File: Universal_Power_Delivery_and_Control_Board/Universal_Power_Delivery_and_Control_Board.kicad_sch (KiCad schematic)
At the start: 1 part

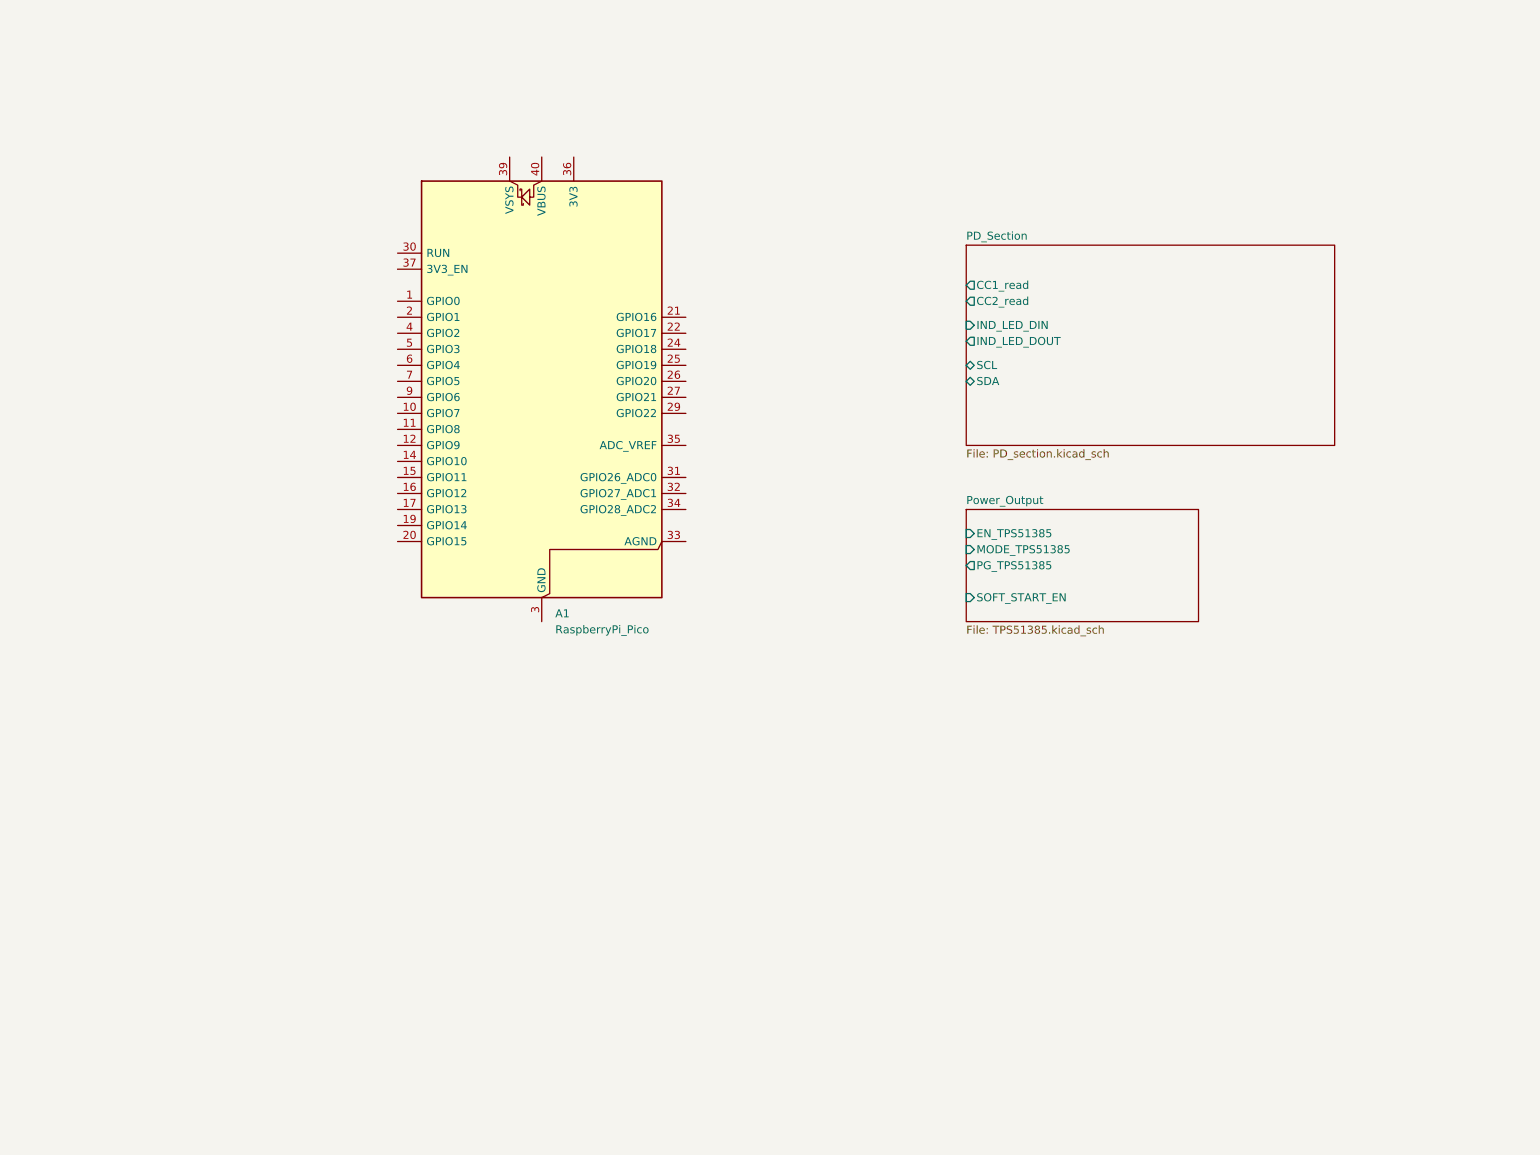
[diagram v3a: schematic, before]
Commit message: Restructured the schematic, added the digital output section and continued with the layout.
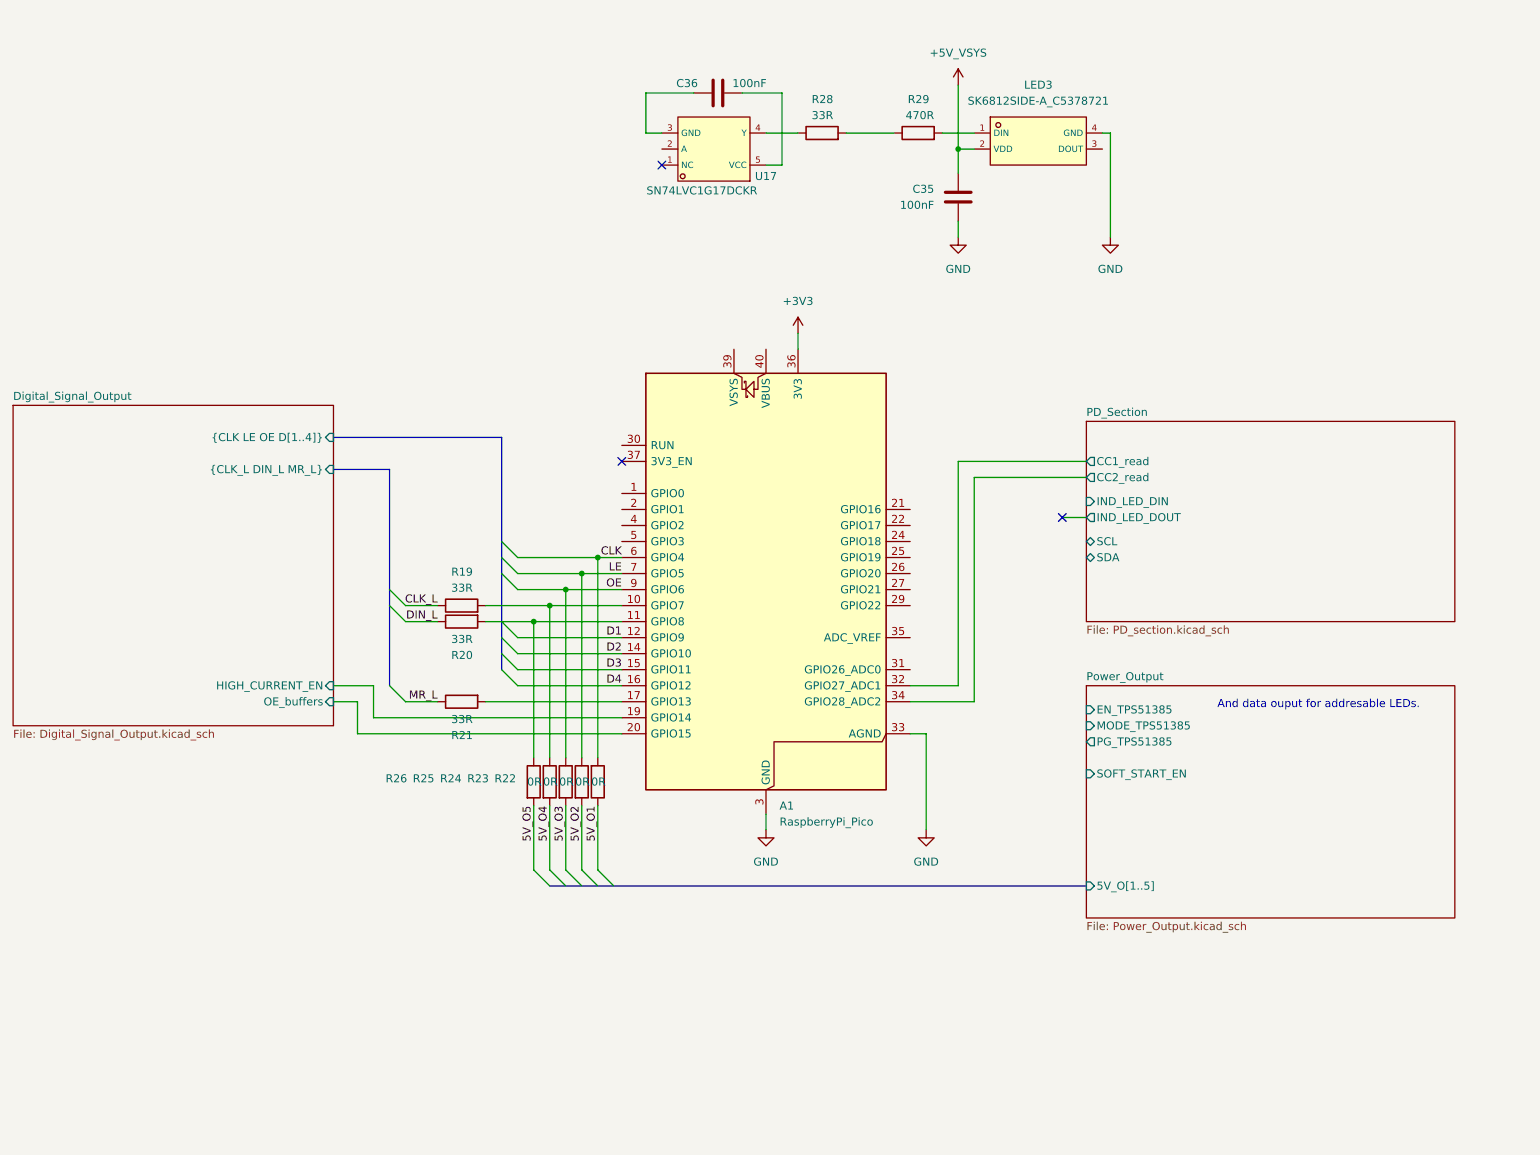
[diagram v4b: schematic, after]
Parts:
- added C35, C36: 100nF, Capacitor_SMD:C_0402_1005Metric_Pad0.74x0.62mm_HandSolder, symbol Device:C
- added LED3: SK6812SIDE-A_C5378721, lcsc_footprints:C5378721_LED-SMD_4P-L4_0-W1_6-L, symbol lcsc_imported:SK6812SIDE-A_C5378721
- added R19, R20, R21, R28: 33R, Resistor_SMD:R_0402_1005Metric_Pad0.72x0.64mm_HandSolder, symbol Device:R
- added R22, R23, R24, R25, R26: 0R, Resistor_SMD:R_0402_1005Metric_Pad0.72x0.64mm_HandSolder, symbol Device:R
- added R29: 470R, Resistor_SMD:R_0402_1005Metric_Pad0.72x0.64mm_HandSolder, symbol Device:R
- added U17: SN74LVC1G17DCKR, lcsc_footprints:C10425_SC-70-5_L2_1-W1_3-P0_65-LS2_1-BR, symbol lcsc_imported:SN74LVC1G17DCKR
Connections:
- net PD_Section/CC1_read: now also A1.32 (GPIO27_ADC1)
- net PD_Section/CC2_read: now also A1.34 (GPIO28_ADC2)
- net at A1.10 (GPIO7): now also R19.2, R25.1
- net at A1.11 (GPIO8): now also R20.2, R26.1
- net D1: now reaches A1.12 (GPIO9)
- net GND: now reaches A1.13 (GND), A1.18 (GND), A1.23 (GND), A1.28 (GND), A1.3 (GND), A1.38 (GND), A1.8 (GND)
- net GND: now also A1.33 (AGND), C35.2, LED3.4 (GND)
- net D2: now reaches A1.14 (GPIO10)
- net D3: now reaches A1.15 (GPIO11)
- net D4: now reaches A1.16 (GPIO12)
- net at A1.17 (GPIO13): now also R21.2
- net Digital_Signal_Output/HIGH_CURRENT_EN: now reaches A1.19 (GPIO14)
- net Digital_Signal_Output/OE_buffers: now reaches A1.20 (GPIO15)
- net +3V3: now reaches A1.36 (3V3)
- net CLK: now reaches A1.6 (GPIO4)
- net CLK: now also R22.2
- net LE: now reaches A1.7 (GPIO5)
- net LE: now also R23.1
- net OE: now reaches A1.9 (GPIO6)
- net OE: now also R24.1
- new net: C36.1, U17.5 (VCC)
- new net: C36.2, U17.3 (GND)
- new net: R28.2, R29.1
- new net: LED3.1 (DIN), R29.2
- new net: R28.1, U17.4 (Y)
- new net +5V_VSYS: C35.1, LED3.2 (VDD)
- new net 5V_O1: R22.1
- new net 5V_O2: R23.2
- new net 5V_O3: R24.2
- new net 5V_O4: R25.2
- new net 5V_O5: R26.2
- new net CLK_L: R19.1
- new net DIN_L: R20.1
- new net MR_L: R21.1
- no-connect marks 0 -> 3
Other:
- added sheet Digital_Signal_Output (Digital_Signal_Output.kicad_sch)
- sheet Power_Output: file TPS51385.kicad_sch -> Power_Output.kicad_sch
- sheet Power_Output ports: added 5V_O[1..5]; removed none
- note added: "And data ouput for addresable LEDs."
- moved on the sheet: A1

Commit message: Switched to a 4 layer stackup and routed the digital output section.
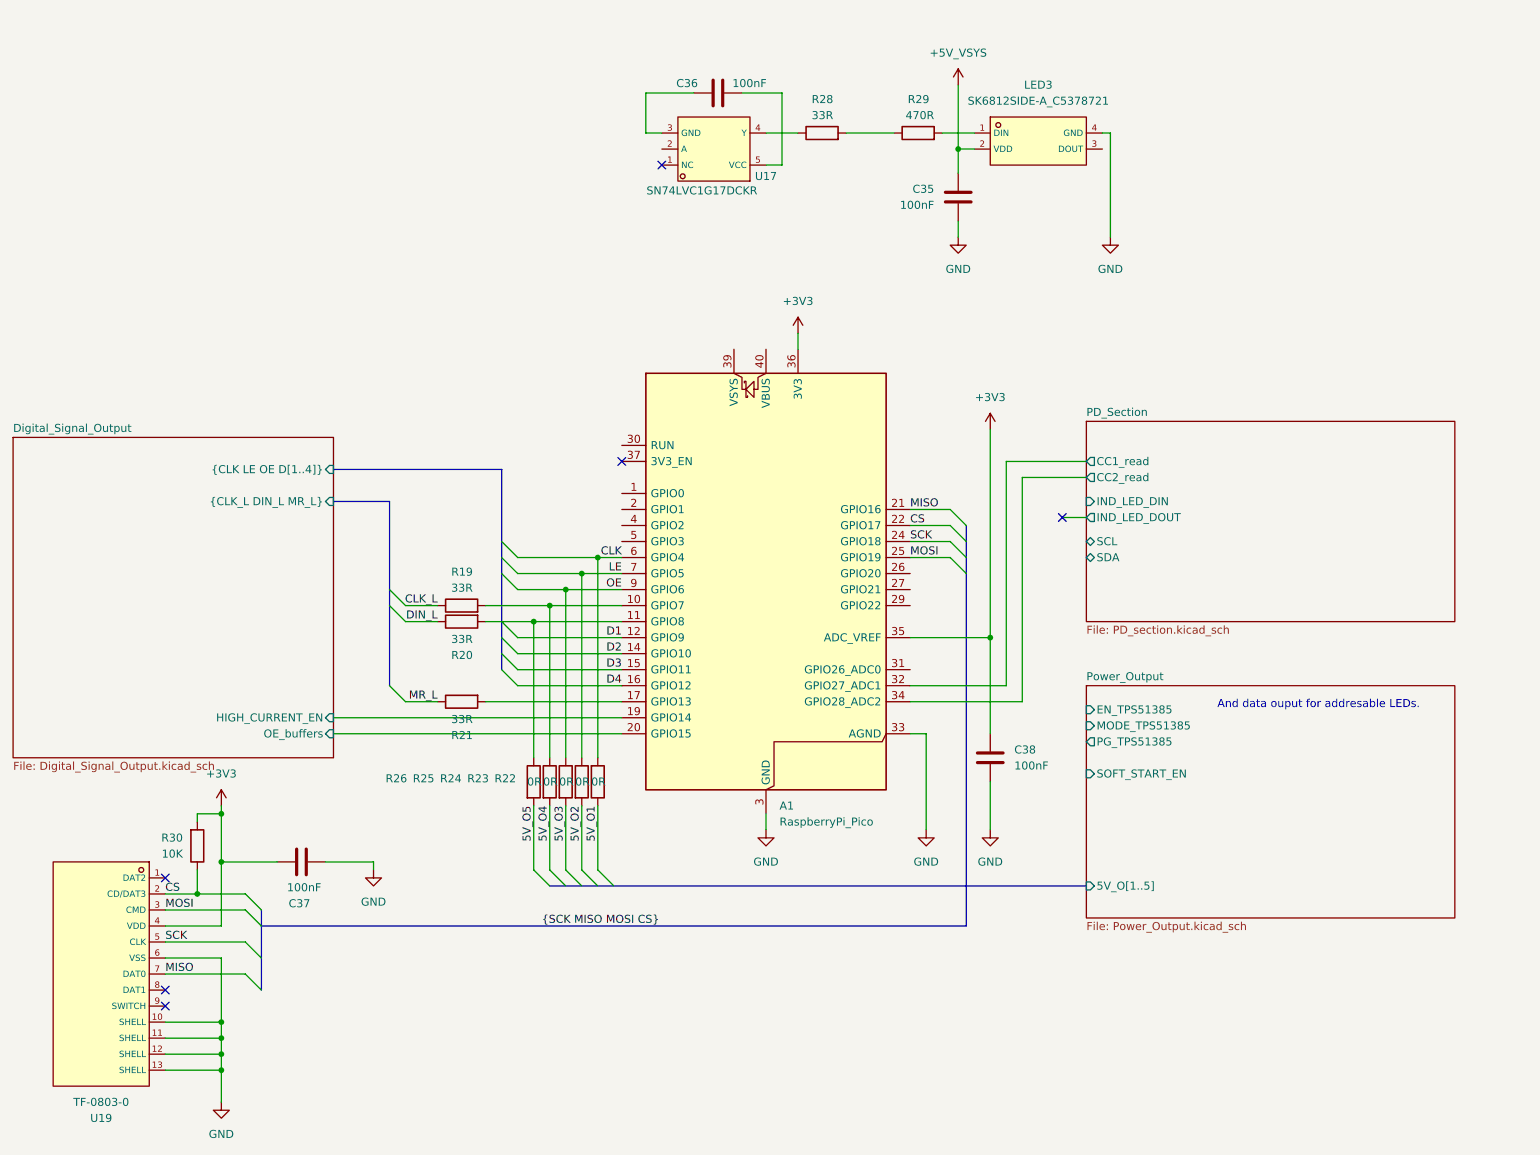
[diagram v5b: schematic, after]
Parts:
- added C37, C38: 100nF, Capacitor_SMD:C_0402_1005Metric_Pad0.74x0.62mm_HandSolder, symbol Device:C
- added R30: 10K, Resistor_SMD:R_0402_1005Metric_Pad0.72x0.64mm_HandSolder, symbol Device:R
- added U19: TF-0803-0, lcsc_footprints:C5362199_TF-SMD_XKTF-0803-0, symbol lcsc_imported:TF-0803-0
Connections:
- net +3V3: now also A1.35 (ADC_VREF), C37.1, C38.1, R30.2, U19.4 (VDD)
- net GND: now also C37.2, C38.2, U19.10 (SHELL), U19.11 (SHELL), U19.12 (SHELL), U19.13 (SHELL), U19.6 (VSS)
- net MISO: now reaches A1.21 (GPIO16)
- net MISO: now also U19.7 (DAT0)
- net CS: now reaches A1.22 (GPIO17)
- net CS: now also R30.1, U19.2 (CD/DAT3)
- net SCK: now reaches A1.24 (GPIO18)
- net SCK: now also U19.5 (CLK)
- net MOSI: now reaches A1.25 (GPIO19)
- net MOSI: now also U19.3 (CMD)
- no-connect marks 3 -> 6

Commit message: Practically finshed the digital output layout, added the i2c io expander as im short on ios.
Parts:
- removed R22, R23, R24, R25, R26: 0R, Resistor_SMD:R_0402_1005Metric_Pad0.72x0.64mm_HandSolder, symbol Device:R
- added C42: 100nF, Capacitor_SMD:C_0402_1005Metric_Pad0.74x0.62mm_HandSolder, symbol Device:C
- added C43: 10uF, Capacitor_SMD:C_0805_2012Metric_Pad1.18x1.45mm_HandSolder, symbol Device:C
- added JP5, JP6: SolderJumper_3_Bridged12, Jumper:SolderJumper-3_P1.3mm_Bridged12_Pad1.0x1.5mm_NumberLabels, symbol Jumper:SolderJumper_3_Bridged12
- added U20: TCA9555PWR, Package_SO:TSSOP-24_4.4x7.8mm_P0.65mm, symbol Interface_Expansion:TCA9555PWR
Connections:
- net CLK is gone; now on net 5V_O1: A1.6 (GPIO4)
- net LE is gone; now on net 5V_O2: A1.7 (GPIO5)
- net OE is gone; now on net 5V_O3: A1.9 (GPIO6)
- net +3V3: now also C42.1, C43.2, JP5.3 (B), JP6.3 (B), U20.24 (VCC)
- net +5V_VSYS: now also A1.39 (VSYS)
- net 5V_O4: now also A1.10 (GPIO7), R19.2
- net 5V_O5: now also A1.11 (GPIO8), R20.2
- net GND: now also C42.2, C43.1, JP5.1 (A), JP6.1 (A), U20.12 (GND), U20.21 (A0)
- net SDA: now reaches A1.1 (GPIO0)
- net SDA: now also U20.22 (SCL)
- net SCL: now reaches A1.2 (GPIO1)
- net SCL: now also U20.23 (SDA)
- net INT: now reaches A1.4 (GPIO2)
- net INT: now also U20.1 (~{INT})
- new net: JP6.2 (C), U20.2 (A1)
- new net: JP5.2 (C), U20.3 (A2)

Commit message: Added some misc stuff layout almost finished.
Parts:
- removed R28: 33R, Resistor_SMD:R_0402_1005Metric_Pad0.72x0.64mm_HandSolder, symbol Device:R
- added R25, R26: 4.7K, Resistor_SMD:R_0402_1005Metric_Pad0.72x0.64mm_HandSolder, symbol Device:R
- added SW2: TS1102-TD35HBM, lcsc_footprints:C36936640_SW-SMD_TS1102-TD35HBM, symbol lcsc_imported:TS1102-TD35HBM
- added U22: HC-PM254-8.5H-2X4PW-02A, lcsc_footprints:C42163146_HDR-TH_8P-P2_54-H-F-R2-C4-S2_54-W8_5, symbol lcsc_imported:HC-PM254-8_5H-2X4PW-02A
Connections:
- net +3V3: now also R25.2, R26.2, U22.2
- net GND: now also U22.1
- net SCL: now also R25.1
- net SDA: now also R26.1
- net at U20.13 (P10): now also U22.4
- net at U20.14 (P11): now also U22.6
- net at U20.15 (P12): now also U22.8
- net at U20.16 (P13): now also U22.7
- net at U20.17 (P14): now also U22.5
- net at U20.18 (P15): now also U22.3
- net P00: now reaches U20.4 (P00)
- net P01: now reaches U20.5 (P01)
- net P02: now reaches U20.6 (P02)
- net P03: now reaches U20.7 (P03)
- net P04: now reaches U20.8 (P04)
- net P05: now reaches U20.9 (P05)
- net SS_EN: now reaches A1.5 (GPIO3)
- net at R29.1: now also U17.4 (Y)
- no-connect marks 6 -> 9
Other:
- moved on the sheet: C35, LED3, R29

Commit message: Practically finished layout, need to route the buttons.
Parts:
- added C47: 100nF, Capacitor_SMD:C_0402_1005Metric_Pad0.74x0.62mm_HandSolder, symbol Device:C
- added R39: 100K, Resistor_SMD:R_0402_1005Metric_Pad0.72x0.64mm_HandSolder, symbol Device:R
- added R40: 10K, Resistor_SMD:R_0402_1005Metric_Pad0.72x0.64mm_HandSolder, symbol Device:R
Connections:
- net +3V3: now also R39.1
- net GND: now also SW2.2, SW2.3, SW2.4, C47.1
- net PD_Section/IND_LED_DIN: now also A1.29 (GPIO22)
- net PD_Section/MAX_current: now reaches A1.26 (GPIO20)
- net PD_Section/H_current: now reaches A1.27 (GPIO21)
- net PD_Section/I_MONITOR: now reaches A1.31 (GPIO26_ADC0)
- net at SW2.1: now also R40.1
- net SS_EN: no longer names the net of A1.5 (GPIO3)
- new net: C47.2, R39.2, R40.2
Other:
- sheet PD_Section ports: added H_current, I_MONITOR, MAX_current, PG_eFUSE, ST_ID; removed none
- moved on the sheet: C35, LED3, R29, SW2
